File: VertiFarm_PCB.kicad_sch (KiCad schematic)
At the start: 33 parts, among them J1 Peltier, J10 Raspberry Pi 5, J11 Peltier, J13 3V3 I2C, J15 3V3 I2C, J17 3V3 I2C, J18 5V I2C, J19 3V3 I2C, J20 Switch_2, J21 Camera, J22 DS12B20, J23 DS12B20, J24 DS12B20, J25 DS12B20, J26 DHT22, J27 DHT22, J33 left, J34 right, J5 Switch_1, J9 5V I2C

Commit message: Version 2.0
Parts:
- added F1: Fuse 15A, Fuse_Blade:Fuse_Blade_ATO_directSolder_32V_15A, symbol Device:Fuse
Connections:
- net +12V: now also F1.1; no longer J11.1 (Pin_1)
- new net: F1.2, J11.1 (Pin_1)
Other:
- moved on the sheet: J11, R27

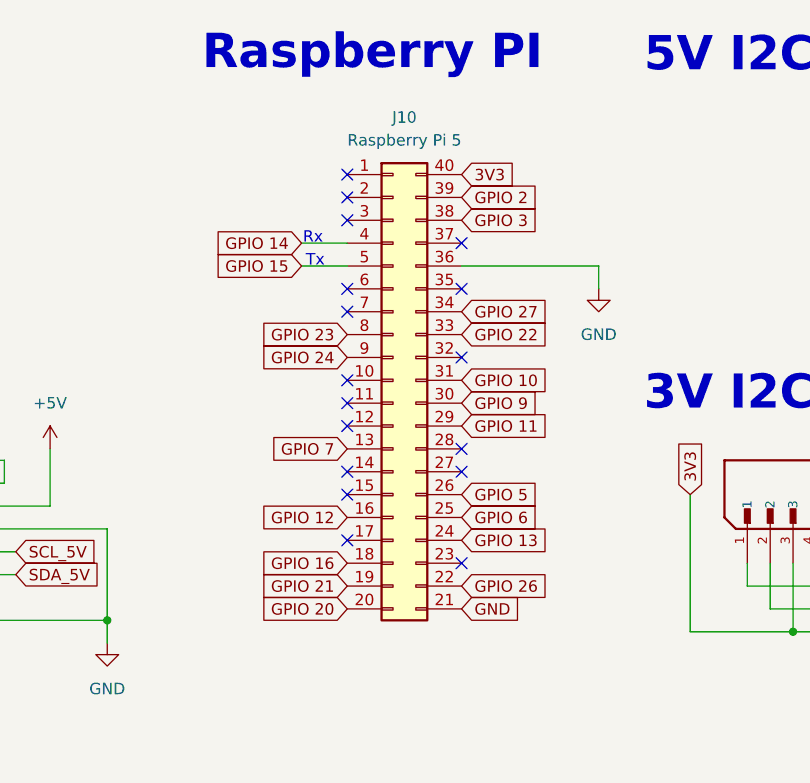
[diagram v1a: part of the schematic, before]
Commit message: Rpi pinouts corrected
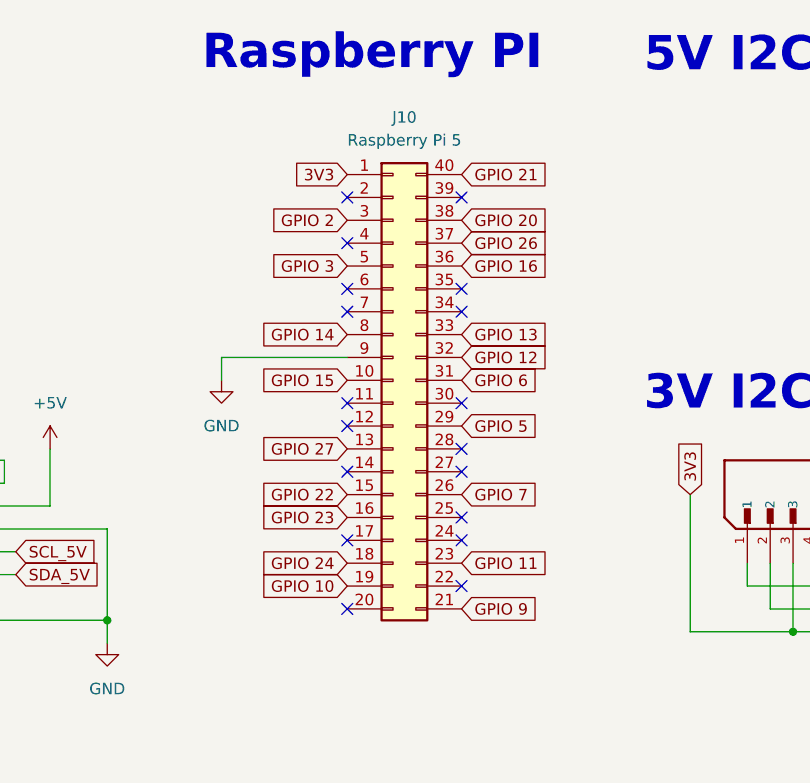
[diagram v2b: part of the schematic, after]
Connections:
- net 3V3: now also J10.1 (Pin_1); no longer J10.40 (Pin_40)
- net GND: now also J10.9 (Pin_9); no longer J10.21 (Pin_21), J10.36 (Pin_36)
- net GPIO 10: now also J10.19 (Pin_19); no longer J10.31 (Pin_31)
- net GPIO 11: now also J10.23 (Pin_23); no longer J10.29 (Pin_29)
- net GPIO 12: now also J10.32 (Pin_32); no longer J10.16 (Pin_16)
- net GPIO 13: now also J10.33 (Pin_33); no longer J10.24 (Pin_24)
- net GPIO 14: now also J10.8 (Pin_8); no longer J10.4 (Pin_4)
- net GPIO 15: now also J10.10 (Pin_10); no longer J10.5 (Pin_5)
- net GPIO 16: now also J10.36 (Pin_36); no longer J10.18 (Pin_18)
- net GPIO 2: now also J10.3 (Pin_3); no longer J10.39 (Pin_39)
- net GPIO 20: now also J10.38 (Pin_38); no longer J10.20 (Pin_20)
- net GPIO 21: now also J10.40 (Pin_40); no longer J10.19 (Pin_19)
- net GPIO 22: now also J10.15 (Pin_15); no longer J10.33 (Pin_33)
- net GPIO 23: now also J10.16 (Pin_16); no longer J10.8 (Pin_8)
- net GPIO 24: now also J10.18 (Pin_18); no longer J10.9 (Pin_9)
- net GPIO 26: now also J10.37 (Pin_37); no longer J10.22 (Pin_22)
- net GPIO 27: now also J10.13 (Pin_13); no longer J10.34 (Pin_34)
- net GPIO 3: now also J10.5 (Pin_5); no longer J10.38 (Pin_38)
- net GPIO 5: now also J10.29 (Pin_29); no longer J10.26 (Pin_26)
- net GPIO 6: now also J10.31 (Pin_31); no longer J10.25 (Pin_25)
- net GPIO 7: now also J10.26 (Pin_26); no longer J10.13 (Pin_13)
- net GPIO 9: now also J10.21 (Pin_21); no longer J10.30 (Pin_30)
- no-connect marks 17 -> 18
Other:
- note removed: "Rx"
- note removed: "Tx"

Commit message: Updated the Fuses Footprints and Corrected Layout
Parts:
- F1: footprint Fuse_Blade:Fuse_Blade_ATO_directSolder_32V_15A -> Footprint:Fuse_Blade_ATO_directSolder_32V_15A

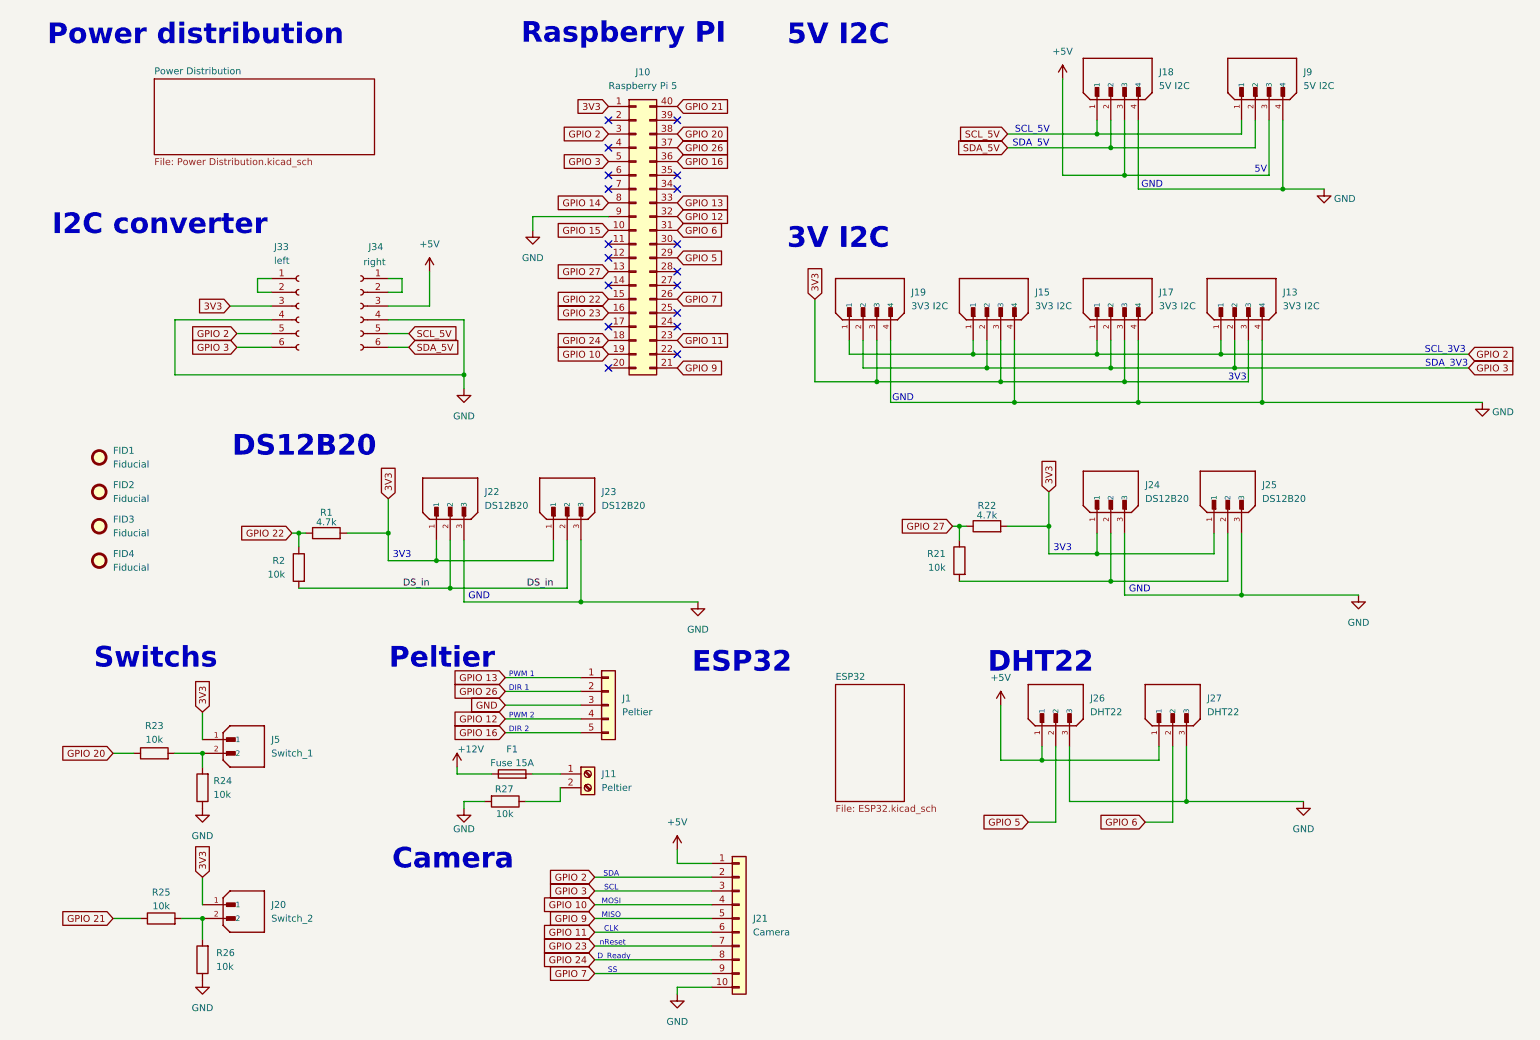
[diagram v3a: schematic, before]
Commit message: updated the connector pins
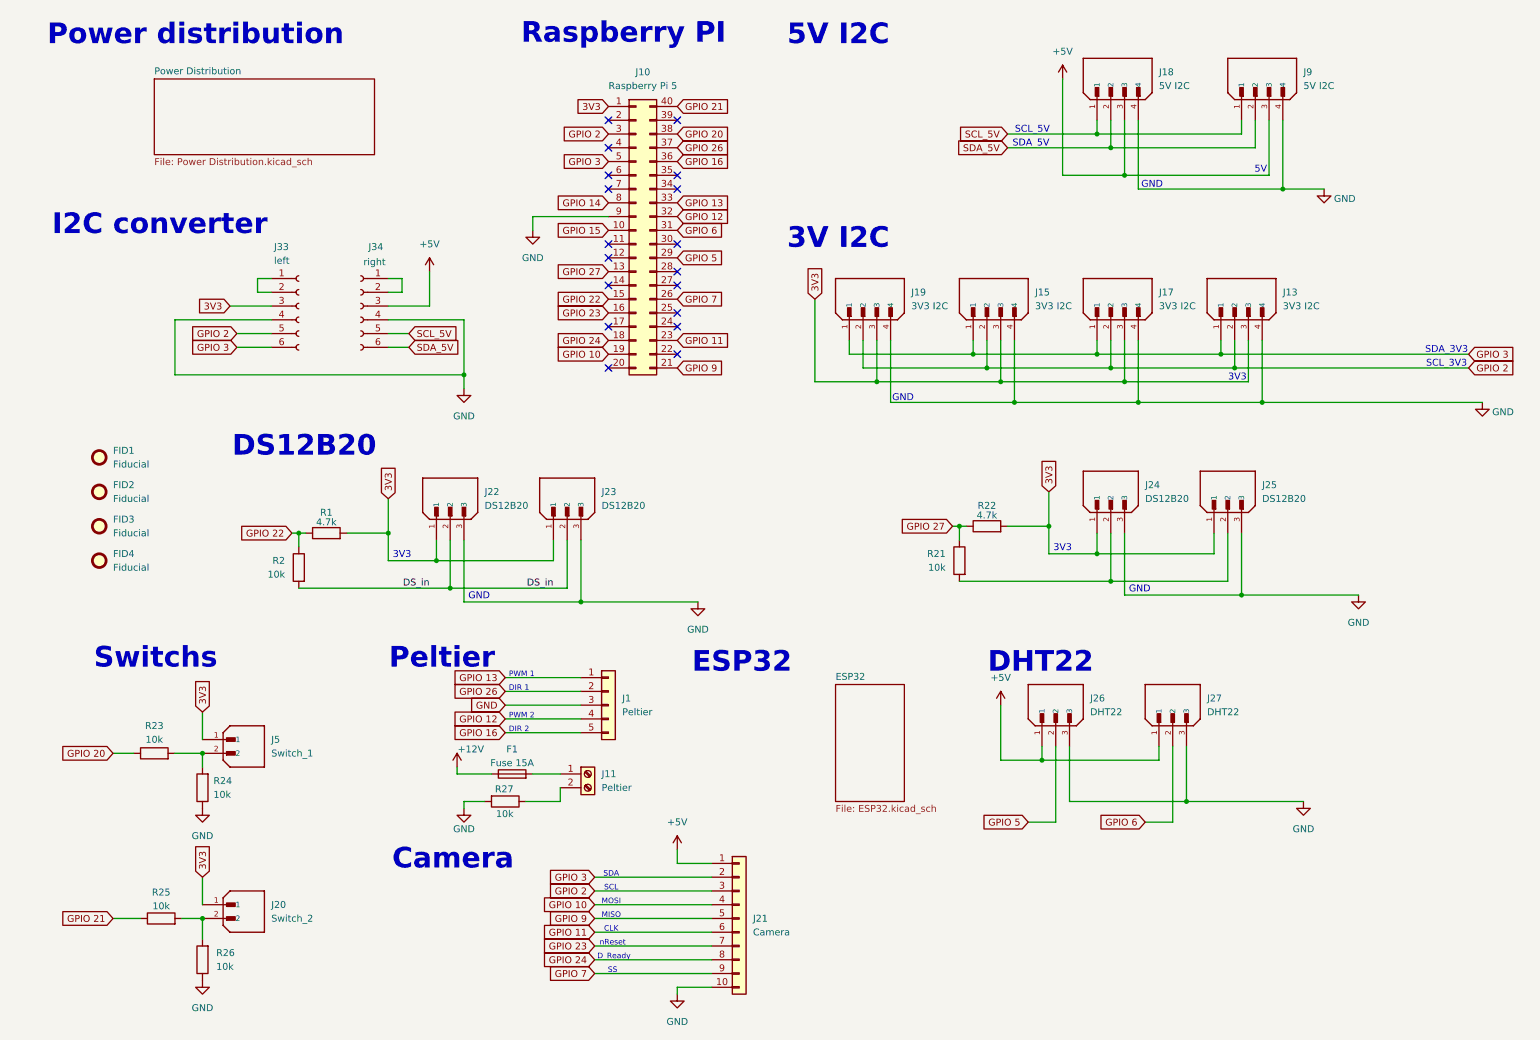
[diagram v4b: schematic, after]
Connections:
- net GPIO 2: now also J13.2, J15.2, J17.2, J19.2, J21.3 (Pin_3); no longer J13.1, J15.1, J17.1, J19.1, J21.2 (Pin_2)
- net GPIO 3: now also J13.1, J15.1, J17.1, J19.1, J21.2 (Pin_2); no longer J13.2, J15.2, J17.2, J19.2, J21.3 (Pin_3)
